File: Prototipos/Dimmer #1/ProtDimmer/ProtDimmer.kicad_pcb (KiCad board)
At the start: 2 copper layers, 114.3 x 83.8 mm, 22 parts, among them J1 Conn_01x02, J2 Conn_01x02, J3 Conn_01x05, K1 SRD-05VDC-SL-C, Q1 BC548B, Q2 BT137, U1 MOC3021M, U2 EL817

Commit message: Primera versión pcb
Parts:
- J3: footprint Connector_PinHeader_2.54mm:PinHeader_1x05_P2.54mm_Vertical -> Connector_PinHeader_2.54mm:PinHeader_1x06_P2.54mm_Vertical
- R3: footprint Resistor_THT:R_Axial_DIN0207_L6.3mm_D2.5mm_P7.62mm_Horizontal -> Potentiometer_THT:Potentiometer_Alps_RK163_Single_Horizontal
- moved D2 56.4 mm to (88.9, 78.7)
- moved C1 55.0 mm to (91.4, 63.5)
- moved D1 48.9 mm to (104.1, 68.6), turned to -90 degrees
- moved D3 48.4 mm to (104.1, 66.0), turned to 90 degrees
- moved R9 45.7 mm to (116.8, 48.3), turned to -90 degrees
- moved R6 45.6 mm to (88.9, 68.6), turned to -90 degrees
- moved R4 35.6 mm to (99.1, 61.0), turned to 180 degrees
- moved R8 34.3 mm to (99.1, 86.4), turned to 90 degrees
- moved R1 34.2 mm to (91.4, 58.4)
- moved R2 33.9 mm to (109.2, 86.4), turned to 90 degrees
- moved U1 33.9 mm to (141.0, 63.5)
- moved R7 33.9 mm to (139.7, 49.5), turned to -90 degrees
- moved C2 32.7 mm to (127.0, 55.9)
- moved R3 28.8 mm to (109.2, 50.8), turned to -90 degrees
- moved J2 28.1 mm to (152.4, 58.4)
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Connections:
- J2 pad 1: Load_N -> 48Vca_N
- J2 pad 2: Load_L -> LOAD_L
- J3 pad 2: UC_PHASE -> UC_DOUT
- J3 pad 3: UC_RELAY -> UC_PHASE
- J3 pad 4: 3.3Vcc -> UC_RELAY
- R3 pad 1: 48Vca_L -> (no net)
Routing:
- net 48Vca_N: track 0.00 -> 133.1 mm, vias 0 -> 2
- net GND: track 0.00 -> 99.1 mm, vias 0 -> 2
- net 48Vca_L: track 0.00 -> 85.3 mm
- net LOAD_L: track 0.00 -> 71.3 mm
- net UC_DOUT: track 0.00 -> 54.9 mm, vias 0 -> 2
- net Net-(K1-Pad3): track 0.00 -> 52.0 mm, vias 0 -> 2
- net RELAY_T2: track 0.00 -> 50.9 mm, vias 0 -> 2
- net UC_PHASE: track 0.00 -> 40.6 mm
- net 5Vcc: track 0.00 -> 26.4 mm
- net Net-(Q1-B): track 0.00 -> 22.9 mm
- net Net-(Q2-G): track 0.00 -> 21.7 mm, vias 0 -> 2
- net Net-(D1-K): track 0.00 -> 20.3 mm
- net Net-(R1-Pad2): track 0.00 -> 15.2 mm
- net Net-(D1-A): track 0.00 -> 10.9 mm
- net Net-(C2-Pad1): track 0.00 -> 10.2 mm
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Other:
- board size 114.3 x 83.8 mm -> 78.7 x 48.3 mm

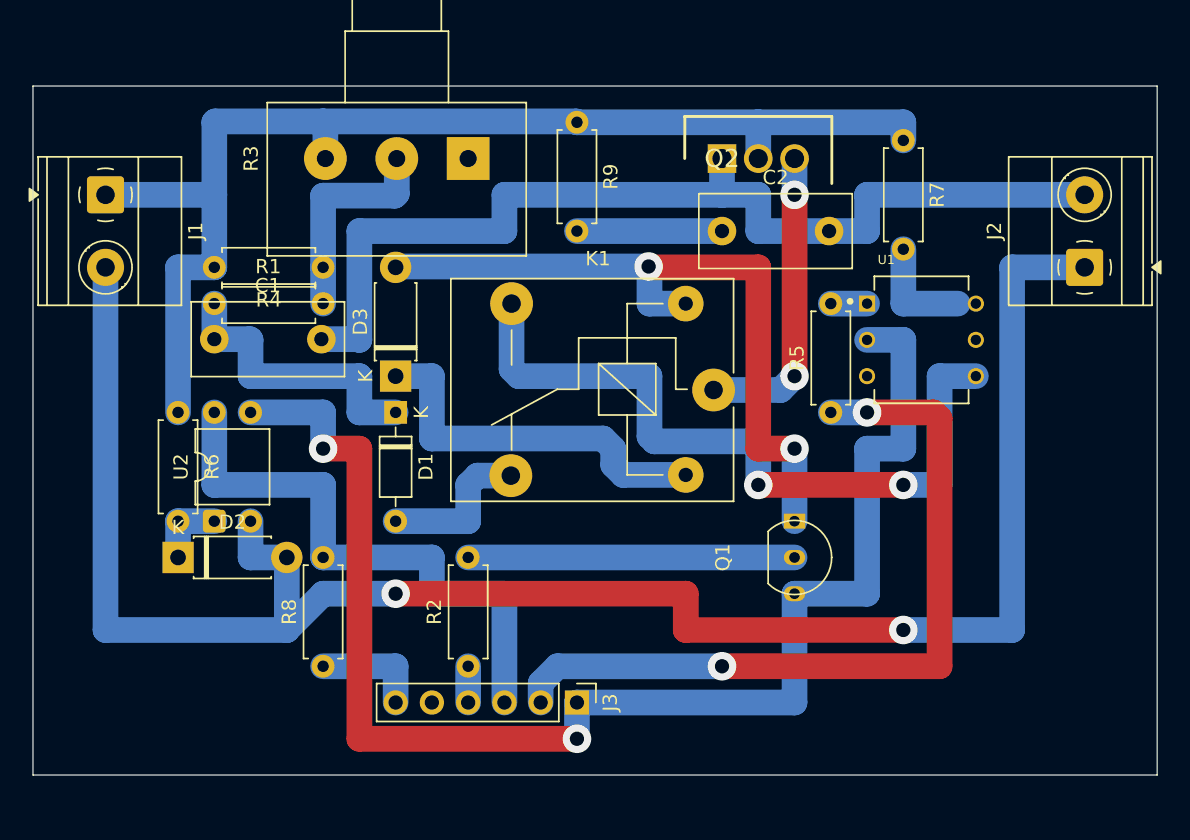
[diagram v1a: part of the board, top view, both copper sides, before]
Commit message: Modificar footprint relé, arreglar conexión faltante
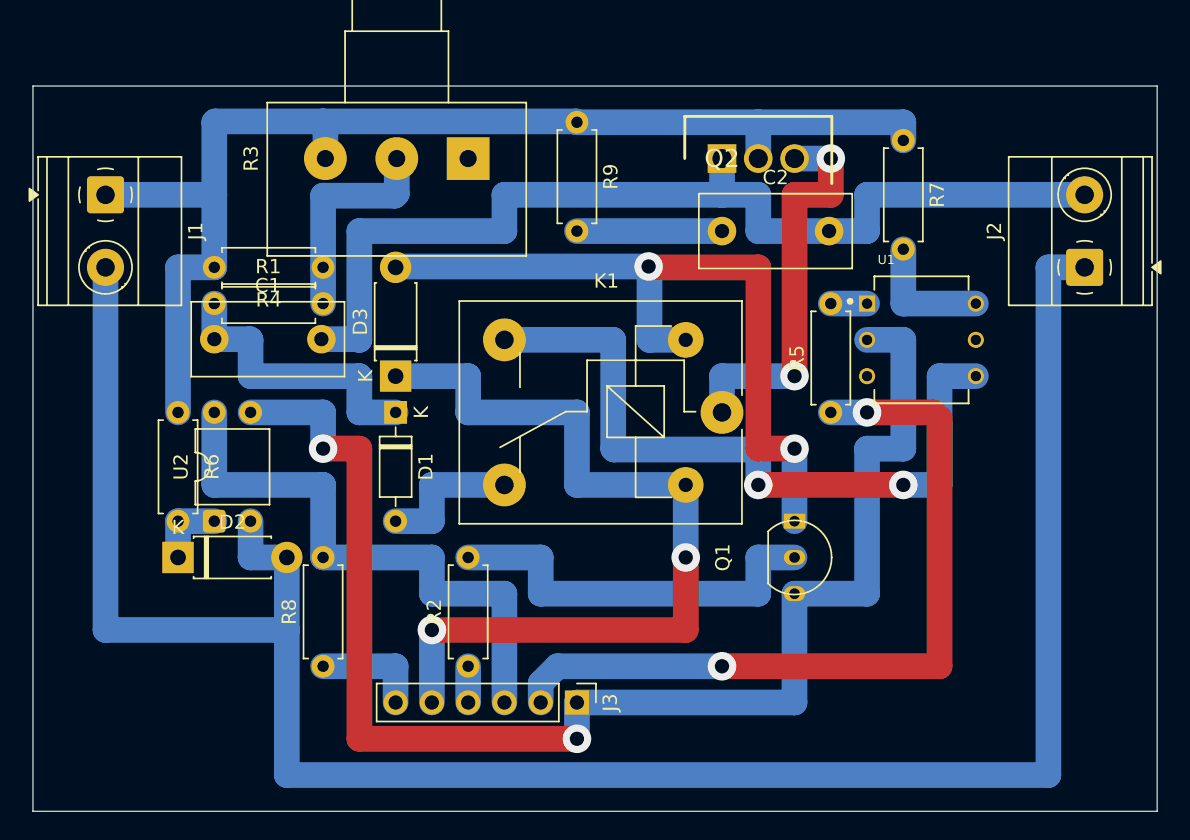
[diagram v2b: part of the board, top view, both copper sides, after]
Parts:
- moved K1 1.68 mm to (127.0, 68.6)
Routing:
- net 5Vcc: track 26.4 -> 61.0 mm, vias 0 -> 2
- net 48Vca_N: track 133.1 -> 149.9 mm, vias 2 -> 0
- net Net-(Q2-G): track 21.7 -> 27.9 mm
- net Net-(Q1-B): track 22.9 -> 27.9 mm
- net RELAY_T2: track 50.9 -> 52.9 mm
- net Net-(R7-Pad2): track 7.62 -> 8.89 mm
- net Net-(K1-Pad3): track 52.0 -> 50.9 mm
- net Net-(D1-A): track 10.9 -> 10.2 mm
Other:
- board size 78.7 x 48.3 mm -> 78.7 x 50.8 mm

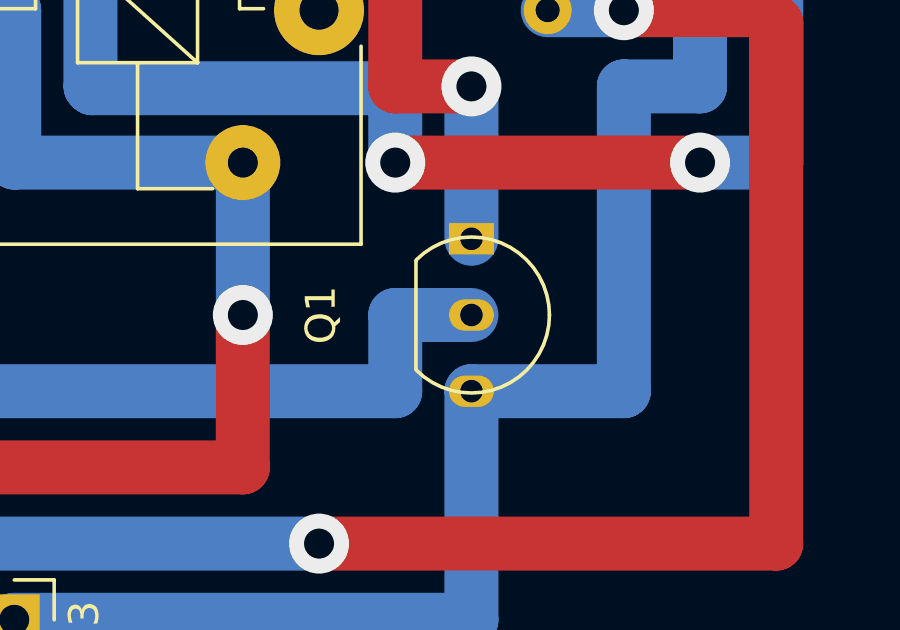
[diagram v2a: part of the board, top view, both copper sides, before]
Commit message: Modificar footprint bc548
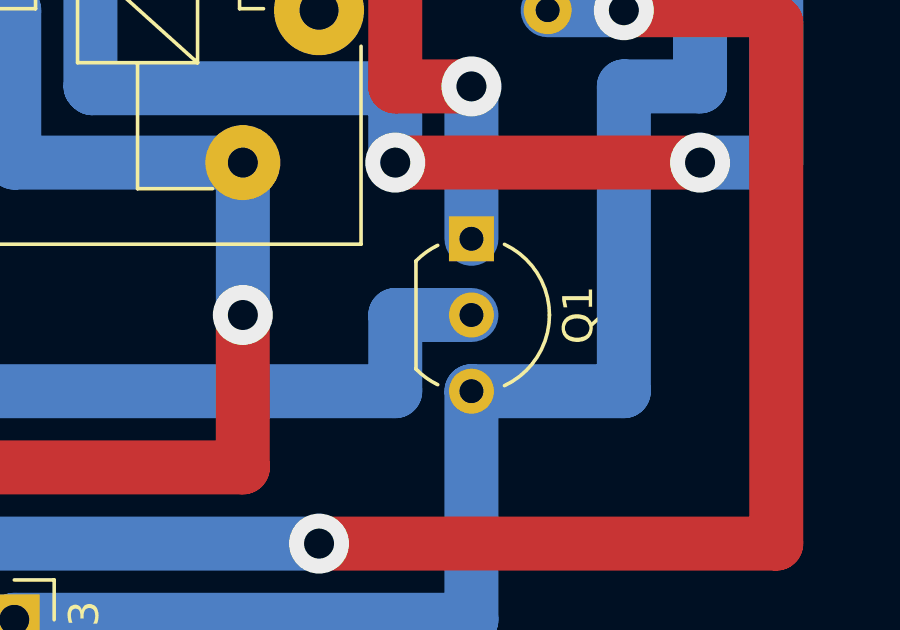
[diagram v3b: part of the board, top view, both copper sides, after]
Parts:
- Q1: footprint Package_TO_SOT_THT:TO-92_Inline -> Package_TO_SOT_THT:TO-92_Inline_Wide
- moved Q1 1.27 mm to (132.1, 76.2)
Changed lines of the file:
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@@
 		)
 	)
-	(footprint "Package_TO_SOT_THT:TO-92_Inline"
+	(footprint "Package_TO_SOT_THT:TO-92_Inline_Wide"
 		(layer "F.Cu")
-		(at 132.08 77.47 -90)
-		(descr "TO-92 leads in-line, narrow, oval pads, drill 0.75mm (see NXP sot054_po.pdf)")
+		(at 132.08 76.2 -90)
+		(descr "TO-92 leads in-line, wide, drill 0.75mm (see NXP sot054_po.pdf)")
 		(tags "to-92 sc-43 sc-43a sot54 PA33 transistor")
 		(property "Reference" "Q1"
-			(at 1.27 5.02 90)
+			(at 2.54 -3.56 270)
 			(layer "F.SilkS")
 			(effects
@@
 		)
 		(property "Value" "BC548B"
-			(at 1.27 2.79 90)
+			(at 2.54 2.79 270)
 			(layer "F.Fab")
 			(effects
@@
 			)
 		)
-		(property "Datasheet" "https://www.onsemi.com/pub/Collateral/BC550-D.pdf"
+		(property "Datasheet" ""
 			(at 0 0 270)
 			(unlocked yes)
@@
 			)
 		)
-		(property "Description" "0.1A Ic, 30V Vce, Small Signal NPN Transistor, TO-92"
+		(property "Description" ""
 			(at 0 0 270)
 			(unlocked yes)
@@
 		(attr through_hole)
 		(fp_line
-			(start -0.53 1.85)
-			(end 3.07 1.85)
-			(stroke
-				(width 0.12)
-				(type solid)
-			)
-			(layer "F.SilkS")
-		)
-		(fp_arc
-			(start -0.568478 1.838478)
-			(mid -1.132087 -0.994977)
-			(end 1.27 -2.6)
-			(stroke
-				(width 0.12)
-				(type solid)
-			)
-			(layer "F.SilkS")
-		)
-		(fp_arc
-			(start 1.27 -2.6)
-			(mid 3.672087 -0.994977)
-			(end 3.108478 1.838478)
-			(stroke
-				(width 0.12)
-				(type solid)
-			)
-			(layer "F.SilkS")
-		)
-		(fp_line
-			(start 4 2.01)
-			(end -1.46 2.01)
-			(stroke
-				(width 0.05)
-				(type solid)
-			)
-			(layer "F.CrtYd")
-		)
-		(fp_line
-			(start 4 2.01)
-			(end 4 -2.73)
-			(stroke
-				(width 0.05)
-				(type solid)
-			)
-			(layer "F.CrtYd")
-		)
-		(fp_line
-			(start -1.46 -2.73)
-			(end -1.46 2.01)
-			(stroke
-				(width 0.05)
-				(type solid)
-			)
-			(layer "F.CrtYd")
-		)
-		(fp_line
-			(start -1.46 -2.73)
-			(end 4 -2.73)
-			(stroke
-				(width 0.05)
-				(type solid)
-			)
-			(layer "F.CrtYd")
-		)
-		(fp_line
-			(start -0.5 1.75)
-			(end 3 1.75)
+			(start 0.74 1.85)
+			(end 4.34 1.85)
+			(stroke
+				(width 0.12)
+				(type solid)
+			)
+			(layer "F.SilkS")
+		)
+		(fp_arc
+			(start 0.74 1.85)
+			(mid 0.446097 1.509328)
+			(end 0.215816 1.122795)
+			(stroke
+				(width 0.12)
+				(type solid)
+			)
+			(layer "F.SilkS")
+		)
+		(fp_arc
+			(start 4.864184 1.122795)
+			(mid 4.633903 1.509328)
+			(end 4.34 1.85)
+			(stroke
+				(width 0.12)
+				(type solid)
+			)
+			(layer "F.SilkS")
+		)
+		(fp_arc
+			(start 0.1836 -1.098807)
+			(mid 1.143021 -2.192817)
+			(end 2.54 -2.6)
+			(stroke
+				(width 0.12)
+				(type solid)
+			)
+			(layer "F.SilkS")
+		)
+		(fp_arc
+			(start 2.54 -2.6)
+			(mid 3.936979 -2.192818)
+			(end 4.8964 -1.098807)
+			(stroke
+				(width 0.12)
+				(type solid)
+			)
+			(layer "F.SilkS")
+		)
+		(fp_line
+			(start 6.09 2.01)
+			(end -1.01 2.01)
+			(stroke
+				(width 0.05)
+				(type solid)
+			)
+			(layer "F.CrtYd")
+		)
+		(fp_line
+			(start 6.09 2.01)
+			(end 6.09 -2.73)
+			(stroke
+				(width 0.05)
+				(type solid)
+			)
+			(layer "F.CrtYd")
+		)
+		(fp_line
+			(start -1.01 -2.73)
+			(end -1.01 2.01)
+			(stroke
+				(width 0.05)
+				(type solid)
+			)
+			(layer "F.CrtYd")
+		)
+		(fp_line
+			(start -1.01 -2.73)
+			(end 6.09 -2.73)
+			(stroke
+				(width 0.05)
+				(type solid)
+			)
+			(layer "F.CrtYd")
+		)
+		(fp_line
+			(start 0.8 1.75)
+			(end 4.3 1.75)
 			(stroke
 				(width 0.1)
@@
 		)
 		(fp_arc
-			(start -0.483625 1.753625)
-			(mid -1.021221 -0.949055)
-			(end 1.27 -2.48)
+			(start 0.786375 1.753625)
+			(mid 0.248779 -0.949055)
+			(end 2.54 -2.48)
 			(stroke
 				(width 0.1)
@@
 		)
 		(fp_arc
-			(start 1.27 -2.48)
-			(mid 3.561221 -0.949055)
-			(end 3.023625 1.753625)
+			(start 2.54 -2.48)
+			(mid 4.831221 -0.949055)
+			(end 4.293625 1.753625)
 			(stroke
 				(width 0.1)
@@
 		)
 		(fp_text user "${REFERENCE}"
-			(at 1.27 0 90)
+			(at 2.54 0 270)
 			(layer "F.Fab")
 			(effects
@@
 		)
 		(pad "1" thru_hole rect
-			(at -1.27 0 270)
-			(size 1.05 1.5)
-			(drill 0.75)
+			(at 0 0 270)
+			(size 1.5 1.5)
+			(drill 0.8)
 			(layers "*.Cu" "*.Mask")
 			(remove_unused_layers no)
@@
 			(pintype "passive")
 		)
-		(pad "2" thru_hole oval
-			(at 1.27 0 270)
-			(size 1.05 1.5)
-			(drill 0.75)
+		(pad "2" thru_hole circle
+			(at 2.54 0 270)
+			(size 1.5 1.5)
+			(drill 0.8)
 			(layers "*.Cu" "*.Mask")
 			(remove_unused_layers no)
@@
 			(pintype "input")
 		)
-		(pad "3" thru_hole oval
-			(at 3.81 0 270)
-			(size 1.05 1.5)
-			(drill 0.75)
+		(pad "3" thru_hole circle
+			(at 5.08 0 270)
+			(size 1.5 1.5)
+			(drill 0.8)
 			(layers "*.Cu" "*.Mask")
 			(remove_unused_layers no)
@@
 		)
 		(embedded_fonts no)
-		(model "${KICAD9_3DMODEL_DIR}/Package_TO_SOT_THT.3dshapes/TO-92_Inline.wrl"
+		(model "${KICAD9_3DMODEL_DIR}/Package_TO_SOT_THT.3dshapes/TO-92_Inline_Wide.wrl"
 			(offset
 				(xyz 0 0 0)

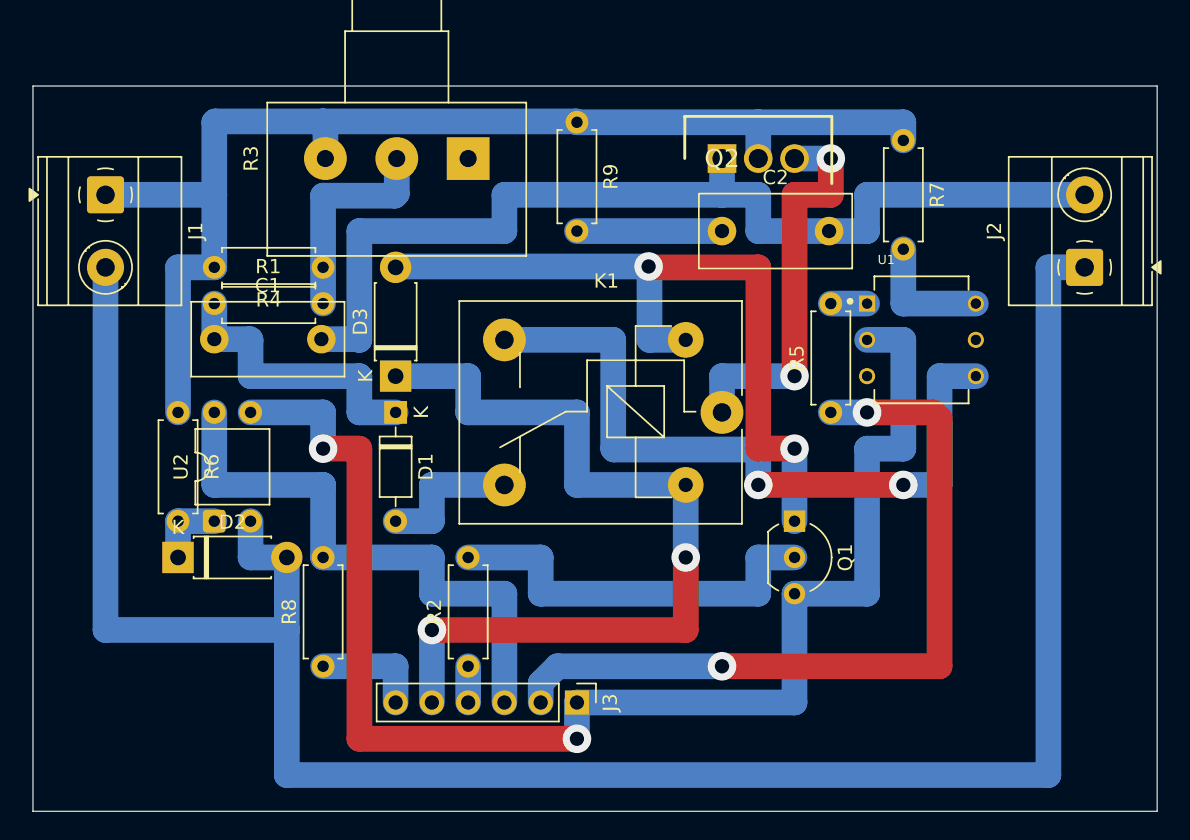
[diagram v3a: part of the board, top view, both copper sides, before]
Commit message: Modificar límites pcb
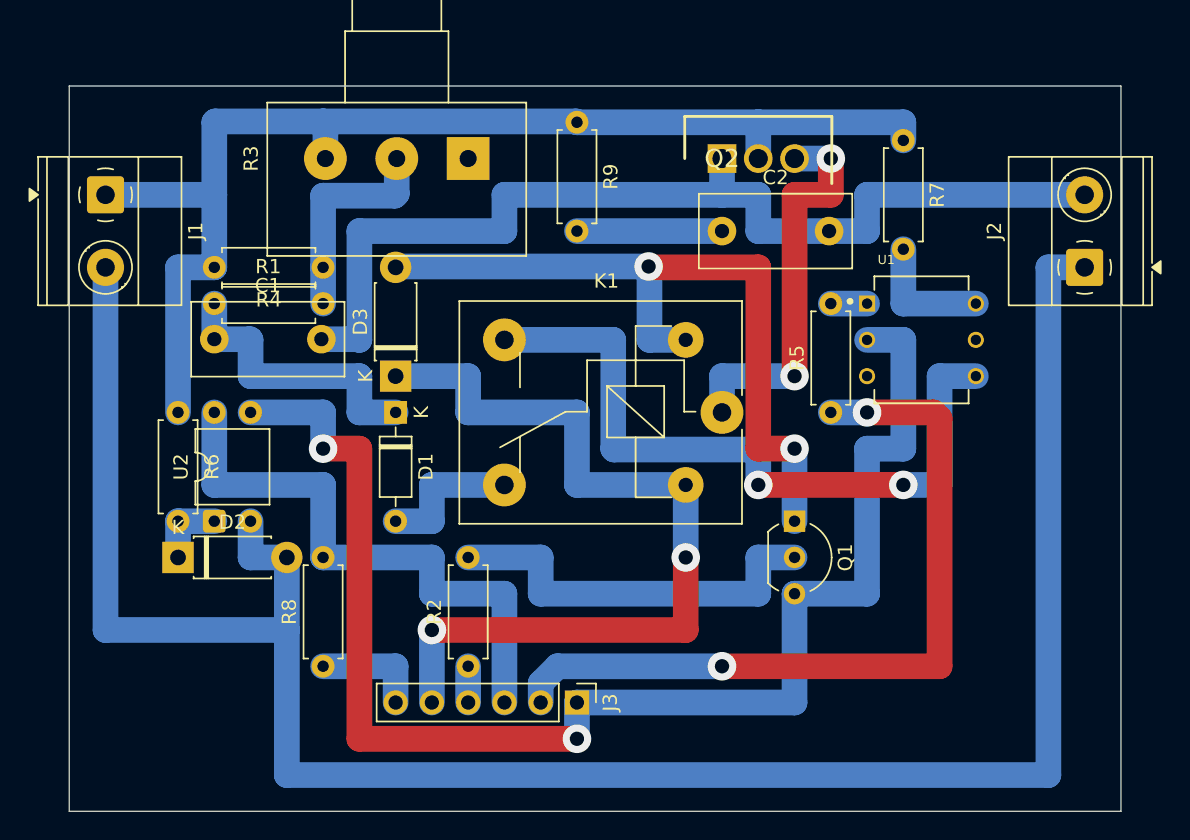
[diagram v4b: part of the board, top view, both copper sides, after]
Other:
- board size 78.7 x 50.8 mm -> 73.7 x 50.8 mm
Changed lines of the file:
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@@
 	)
 	(gr_line
-		(start 157.48 45.72)
-		(end 78.74 45.72)
+		(start 154.94 45.72)
+		(end 81.28 45.72)
 		(stroke
 			(width 0.05)
@@
 	)
 	(gr_line
-		(start 157.48 96.52)
-		(end 157.48 45.72)
+		(start 154.94 96.52)
+		(end 154.94 45.72)
 		(stroke
 			(width 0.05)
@@
 	)
 	(gr_line
-		(start 78.74 96.52)
-		(end 157.48 96.52)
+		(start 81.28 96.52)
+		(end 154.94 96.52)
 		(stroke
 			(width 0.05)
@@
 	)
 	(gr_line
-		(start 78.74 45.72)
-		(end 78.74 96.52)
+		(start 81.28 45.72)
+		(end 81.28 96.52)
 		(stroke
 			(width 0.05)
